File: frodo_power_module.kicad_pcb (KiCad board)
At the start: 2 copper layers, 56 x 71.2 mm, 71 parts, among them J1 Keystone 1098, J10 SWD Header, J2 Molex MicroFit 2x2, J3 Molex MicroFit 2x2, J4 Molex MicroFit 2x2, J5 Molex MicroFit 2x2, J6 Molex MicroFit 2x2, J7 JST-GH, J8 JST-GH, J9 JST-GH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

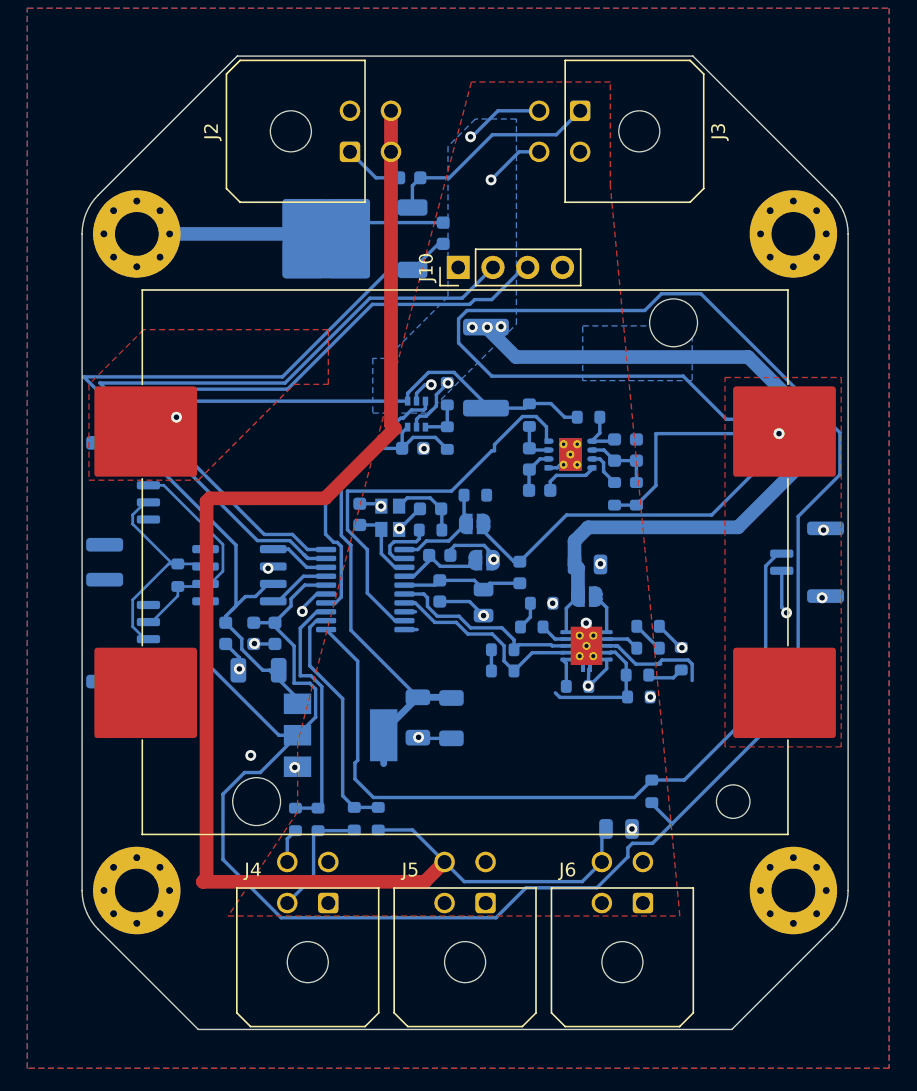
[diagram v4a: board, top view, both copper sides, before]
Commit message: Update PCB design, add LEDs
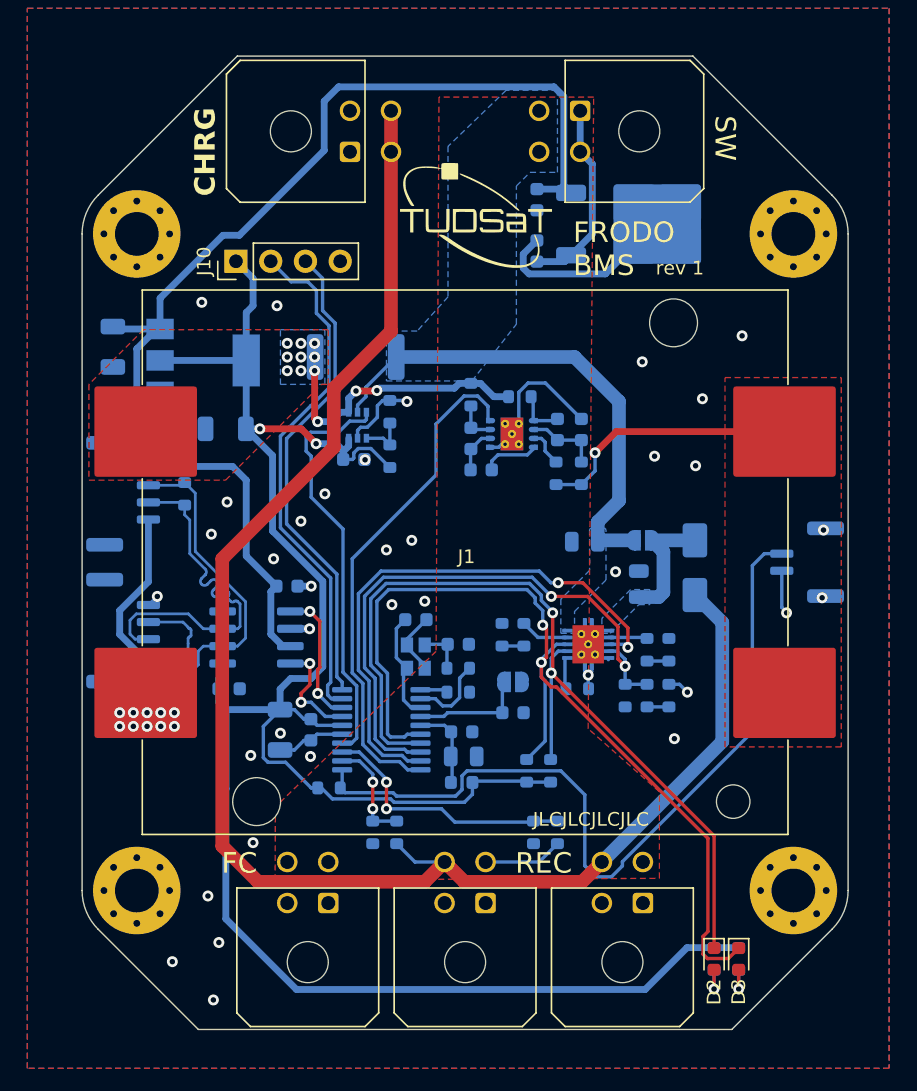
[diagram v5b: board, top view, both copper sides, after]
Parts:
- removed JP3: SolderJumper_2_Open, Jumper:SolderJumper-2_P1.3mm_Open_RoundedPad1.0x1.5mm
- added D1: ~, Diode_SMD:D_SMA, B.Cu at (140.8, 124.4)
- added D2: green, LED_SMD:LED_0603_1608Metric, F.Cu at (142.2, 153.0)
- added D3: red, LED_SMD:LED_0603_1608Metric, F.Cu at (144.0, 153.0)
- added R25: 1k, Resistor_SMD:R_0603_1608Metric, B.Cu at (142.2, 153.0)
- added R26: 1k, Resistor_SMD:R_0603_1608Metric, B.Cu at (144.0, 153.0)
- moved U3 29.2 mm to (104.8, 109.2)
- moved C4 26.8 mm to (106.5, 114.2), turned to 0 degrees
- moved C3 25.9 mm to (98.2, 108.2), turned to 90 degrees
- moved R2 23.6 mm to (114.0, 140.5), turned to 0 degrees
- moved U2 21.7 mm to (136.8, 99.3), turned to 0 degrees
- moved R22 19.2 mm to (130.8, 143.8)
- moved C12 18.0 mm to (136.7, 125.6), turned to 90 degrees
- moved J10 16.3 mm to (107.2, 102.0)
- moved L1 15.9 mm to (123.8, 140.1), turned to 180 degrees
- moved R23 15.8 mm to (129.0, 143.8)
- moved R4 14.5 mm to (123.5, 133.5)
- moved C11 12.7 mm to (127.5, 135.0)
- moved C7 11.3 mm to (123.9, 138.2), turned to 180 degrees
- moved C1 10.7 mm to (129.2, 101.2), turned to -90 degrees
- moved C8 10.4 mm to (123.8, 136.4), turned to 180 degrees
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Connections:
- C12 pad 1: VDC -> Net-(D1-K)
- U1 pad 10: CHARGE_ENABLE -> BLNCR_OUT
- U1 pad 9: BLNCR_OUT -> CHARGE_ENABLE
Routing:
- net +3V3: track 244.9 -> 155.4 mm, vias 0 -> 2
- net STAT2: track 14.5 -> 69.9 mm, vias 0 -> 2
- net STAT1: track 14.8 -> 66.4 mm, vias 0 -> 2
- net +BATT: track 70.8 -> 36.4 mm, vias 6 -> 0
- net NTC: track 10.2 -> 43.1 mm, vias 0 -> 2
- net CHARGE_ENABLE: track 9.10 -> 40.5 mm, vias 0 -> 2
- net GND: track 75.4 -> 51.7 mm, vias 23 -> 46
- net +5V: track 66.1 -> 85.1 mm
- net SWCLK: track 53.6 -> 35.4 mm
- net SWDIO: track 54.5 -> 38.4 mm
- net Net-(J1-Pin_1): track 32.8 -> 20.1 mm, vias 1 -> 12
- net Net-(J7-Pin_1): track 0.00 -> 12.0 mm
- net CAN-: track 16.6 -> 27.8 mm
- net CAN+: track 16.7 -> 27.7 mm
- net VDC: track 106.8 -> 117.5 mm
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- added copper zone on B.Cu, net Net-(D1-K)
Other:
- board text added: "FRODO BMS"
- board text added: "JLCJLCJLCJLC"
- board text added: "rev 1"

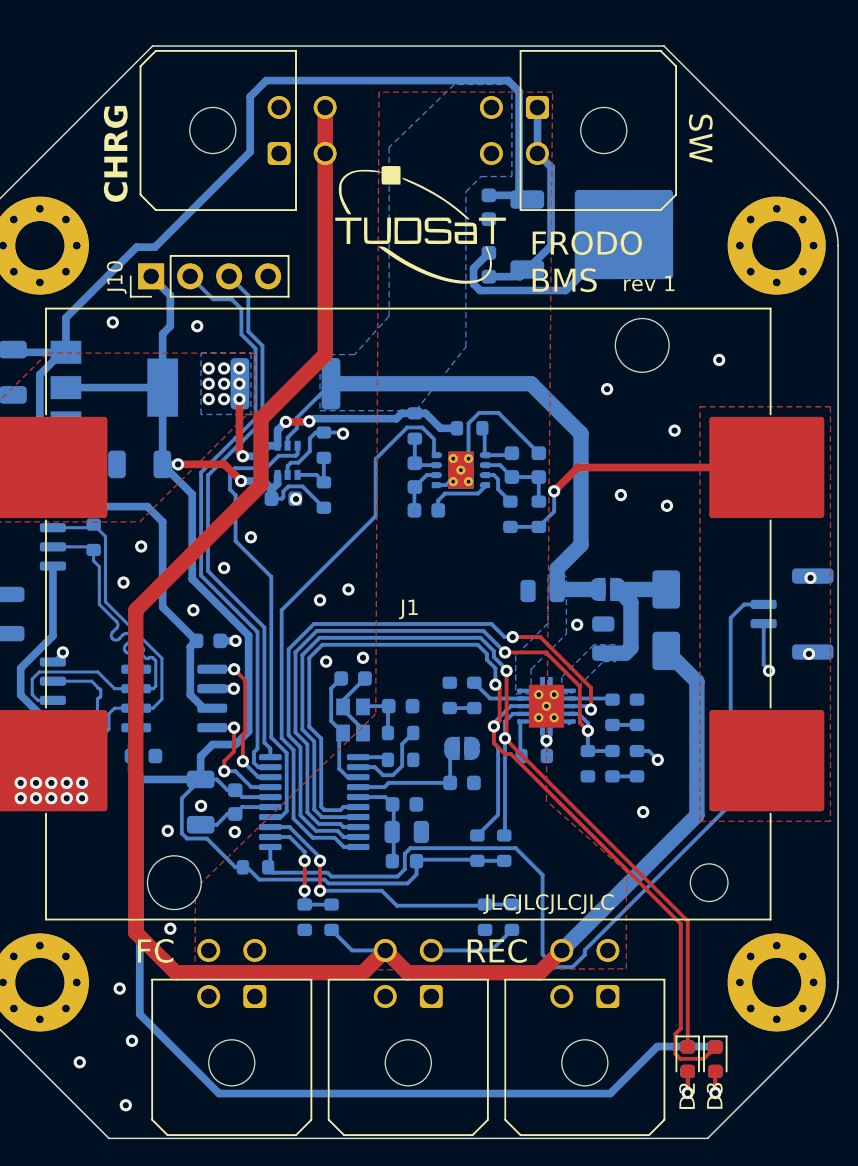
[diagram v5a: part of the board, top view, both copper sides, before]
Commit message: Add fuses to outputs, finish BOM
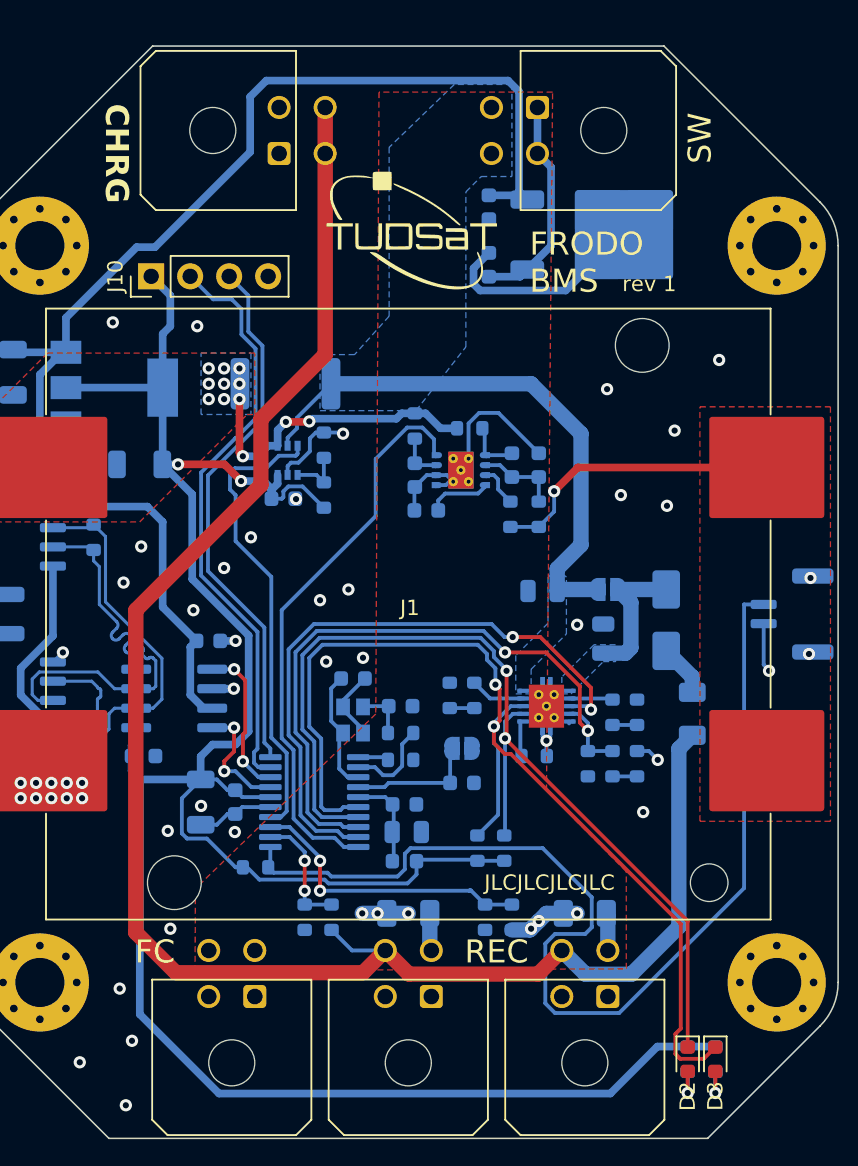
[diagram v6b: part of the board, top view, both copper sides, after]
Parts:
- added F1: 1.5A, Fuse:Fuse_1206_3216Metric, B.Cu at (142.5, 130.5)
- added F2: 1.5A, Fuse:Fuse_1206_3216Metric, B.Cu at (124.0, 143.5)
- added F3: 1.5A, Fuse:Fuse_1206_3216Metric, B.Cu at (135.5, 143.5)
- C10, C9: value TODO -> 10p
- R3: value TODO -> 1k
- Y1: value 8MHz -> 8MHz, 12p
- turned C2 to -90 degrees
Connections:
- C2 pad 1: GND -> +5V
- C2 pad 2: +5V -> GND
- D1 pad 2: VDC -> Net-(D1-A)
- J5 pad 3: +VSW -> Net-(J5-Pin_3)
- J6 pad 3: +VSW -> Net-(J6-Pin_3)
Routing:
- net BREAKWIRE: track 58.6 -> 71.1 mm
- net Net-(D1-A): track 0.00 -> 3.40 mm
- net Net-(J6-Pin_3): track 0.00 -> 2.46 mm
- net Net-(J5-Pin_3): track 0.00 -> 2.46 mm
- net +VSW: track 20.1 -> 22.0 mm, vias 0 -> 6
- net VDC: track 117.5 -> 116.0 mm
- net GND: track 51.7 -> 52.9 mm
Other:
- board text removed: "TODOs: - Silkscreen - Infos for Connectors - Name & rev - JLCJLCJLCJLC"

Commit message: worked on pcb
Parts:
- removed F2, F3: 1.5A, Fuse:Fuse_1206_3216Metric
- removed J8: JST-GH, Connector_JST:JST_GH_SM04B-GHS-TB_1x04-1MP_P1.25mm_Horizontal
- removed J9: JST-GH, Connector_JST:JST_GH_SM02B-GHS-TB_1x02-1MP_P1.25mm_Horizontal
- removed R11, R12, R2: 10k, Resistor_SMD:R_0603_1608Metric
- added D5: 3V9, footprints:SOD323F_DIO-L, B.Cu at (125.0, 113.1)
- added D6: 3V9, footprints:SOD323F_DIO-L, B.Cu at (123.3, 113.0)
- added JP3: SolderJumper_2_Open, Jumper:SolderJumper-2_P1.3mm_Open_RoundedPad1.0x1.5mm, F.Cu at (144.8, 78.3)
- added R27: 22k, Resistor_SMD:R_0603_1608Metric, B.Cu at (124.1, 108.6)
- added R28: 22k, Resistor_SMD:R_0603_1608Metric, B.Cu at (124.1, 110.2)
- C1, C2, C3, C4, JP2, R10, TH1, U2, U3: moved to F.Cu
- D2, D3: moved to B.Cu
- J1: value Keystone 1098 -> Keystone 1048; footprint frodo_power_module:keystone_1098 -> frodo_power_module:keystone_1048
- J2: value Molex MicroFit 2x2 -> Molex MicroFit 2x3; footprint Connector_Molex:Molex_Micro-Fit_3.0_43045-0400_2x02_P3.00mm_Horizontal -> Connector_Molex:Molex_Micro-Fit_3.0_43045-0612_2x03_P3.00mm_Vertical
- J5, J6: value Molex MicroFit 2x2 -> JST-GH; footprint Connector_Molex:Molex_Micro-Fit_3.0_43045-0400_2x02_P3.00mm_Horizontal -> Connector_JST:JST_GH_SM04B-GHS-TB_1x04-1MP_P1.25mm_Horizontal
- J7: value JST-GH -> Molex MicroFit 2x3; footprint Connector_JST:JST_GH_SM04B-GHS-TB_1x04-1MP_P1.25mm_Horizontal -> Connector_Molex:Molex_Micro-Fit_3.0_43045-0612_2x03_P3.00mm_Vertical; moved to F.Cu
- R25, R26: value 1k -> 1k5
- R7: value 220 -> 1k
- R8: value 220 -> 680
- moved J6 76.0 mm to (151.7, 74.3)
- moved J5 74.8 mm to (136.6, 74.9)
- moved JP2 59.8 mm to (144.7, 75.5)
- moved C5 56.6 mm to (123.7, 81.2), turned to -90 degrees
- moved R26 51.2 mm to (116.9, 109.6), turned to 90 degrees
- moved R25 51.1 mm to (115.3, 109.5)
- moved D3 48.5 mm to (116.9, 112.7), turned to 90 degrees
- moved D2 48.4 mm to (115.3, 112.7), turned to 90 degrees
- moved C19 45.8 mm to (126.5, 82.6)
- moved U6 45.6 mm to (123.8, 86.5)
- moved J7 45.4 mm to (92.0, 74.1), turned to 0 degrees
- moved F1 43.9 mm to (104.5, 108.4), turned to 0 degrees
- moved C6 43.3 mm to (127.6, 95.6), turned to -90 degrees
- moved R22 41.7 mm to (114.7, 105.2), turned to 0 degrees
- moved R20 40.4 mm to (103.9, 106.3), turned to 0 degrees
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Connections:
- D2 pad 1: STAT1 -> Net-(D2-K)
- D3 pad 1: STAT2 -> Net-(D3-K)
- J2 pad 3: VDC -> Net-(J2-Pin_3)
- J5 pad 1: GND -> unconnected-(J5-Pin_1-Pad1)
- J5 pad 2: GND -> CAN+
- J5 pad 3: Net-(J5-Pin_3) -> CAN-
- J5 pad 4: VDC -> GND
- J6 pad 1: GND -> unconnected-(J6-Pin_1-Pad1)
- J6 pad 2: GND -> Net-(J2-Pin_6)
- J6 pad 3: Net-(J6-Pin_3) -> Net-(J2-Pin_3)
- J6 pad 4: VDC -> GND
- J7 pad 1: Net-(J7-Pin_1) -> GND
- J7 pad 2: CAN+ -> GND
- J7 pad 4: GND -> VDC
- JP1 pad 1: Net-(D1-K) -> NRST
- JP1 pad 2: +BATT -> GND
- JP2 pad 1: NRST -> CAN+
- JP2 pad 2: GND -> Net-(J2-Pin_6)
- R25 pad 1: +3V3 -> Net-(D1-K)
- R26 pad 1: +3V3 -> Net-(D1-K)
- R7 pad 2: Net-(R7-Pad2) -> GND
- R8 pad 1: Net-(R7-Pad2) -> Net-(U4-ISET)
- U1 pad 11: BREAKWIRE -> unconnected-(U1-PA5-Pad11)
- U4 pad 7: STAT1 -> Net-(D2-K)
- U4 pad 8: STAT2 -> Net-(D3-K)
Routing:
- net GND: track 52.9 -> 227.3 mm, vias 46 -> 22
- net +VSW: track 22.0 -> 142.3 mm, vias 6 -> 0
- net Net-(J2-Pin_6): track 0.00 -> 110.9 mm
- net Net-(J2-Pin_3): track 0.00 -> 104.8 mm
- net Net-(J1-Pin_2): track 19.1 -> 102.3 mm
- net BREAKWIRE: track 71.1 -> 0.00 mm
- net STAT2: track 69.9 -> 15.1 mm, vias 2 -> 0
- net STAT1: track 66.4 -> 13.4 mm, vias 2 -> 0
- net +5V: track 85.1 -> 32.9 mm, vias 0 -> 1
- net NTC: track 43.1 -> 93.3 mm
- net CHARGE_ENABLE: track 40.5 -> 90.6 mm
- net BLNCR_OUT: track 37.3 -> 86.5 mm
- net CAN-: track 27.8 -> 75.6 mm, vias 0 -> 2
- net +3V3: track 155.4 -> 108.3 mm, vias 2 -> 12
- net CAN+: track 27.7 -> 71.9 mm, vias 0 -> 5
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- added copper zone on F.Cu, net +3V3
- added copper zone on F.Cu, net +BATT
- removed copper zone on F.Cu, net +VSW
- removed copper zone on B.Cu, net GND
- removed copper zone on B.Cu, net Net-(D1-K)
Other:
- board size 56 x 71.2 mm -> 96.2 x 69 mm
- board text removed: "FRODO BMS"
- board text removed: "JLCJLCJLCJLC"
- board text removed: "rev 1"
